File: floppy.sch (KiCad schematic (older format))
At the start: 4 parts, among them CN11 INTERNAL_FLOPPY, CN12 FLOPPY_POWER, U36 74LS05, U5 GARY_5719

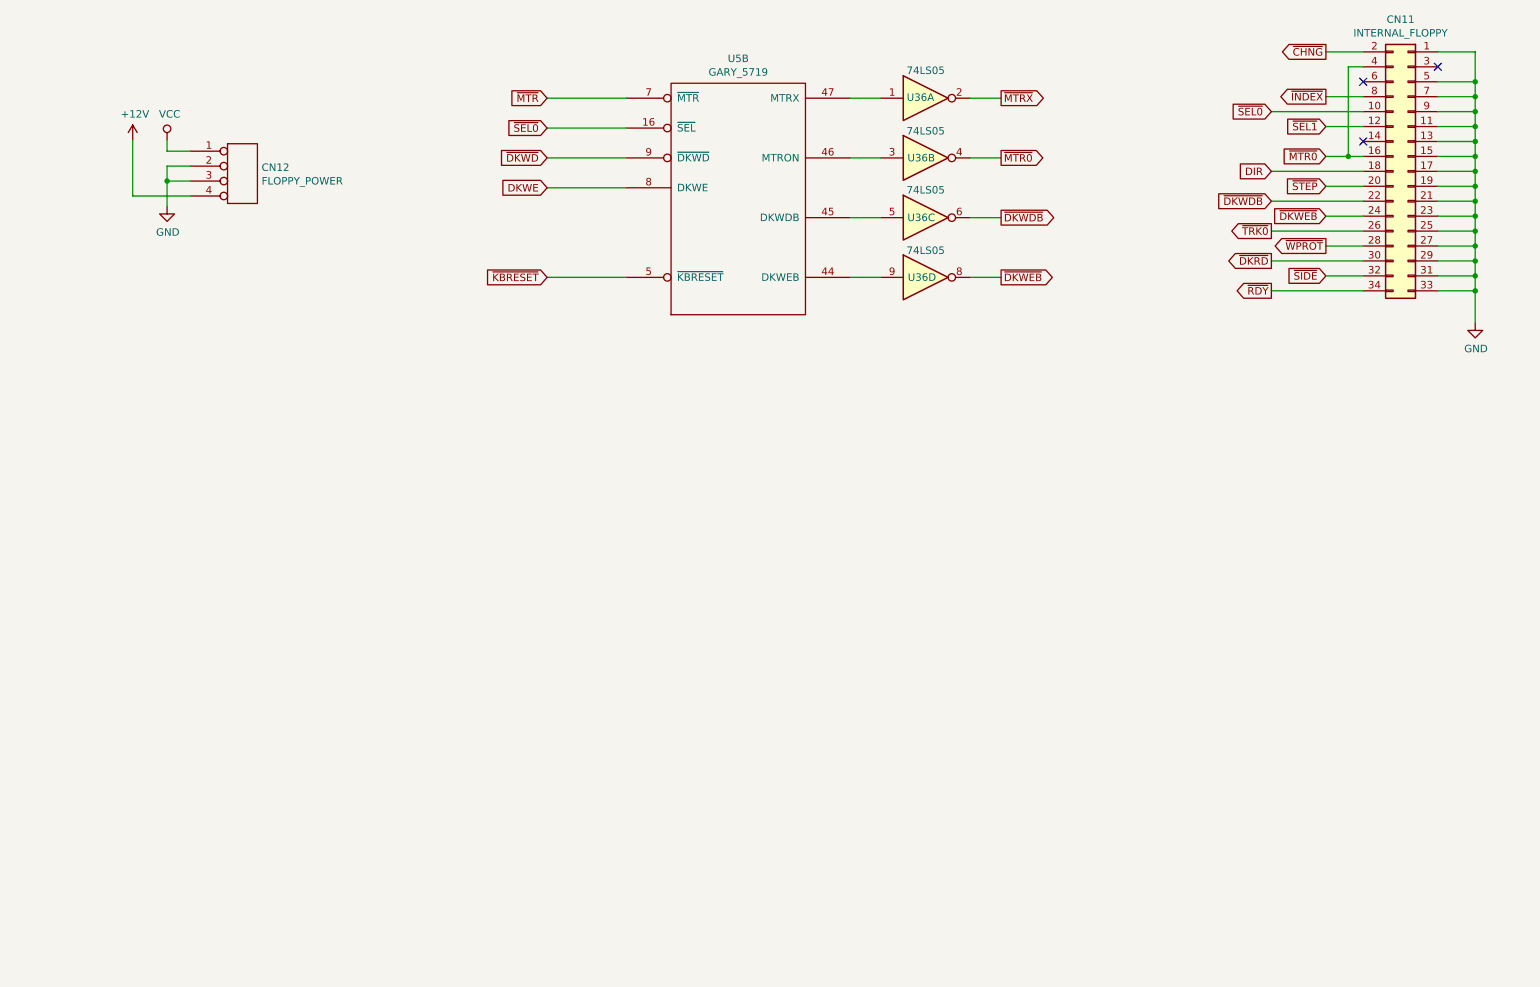
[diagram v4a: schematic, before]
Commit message: Add external floppy connector (and do a few fixes)
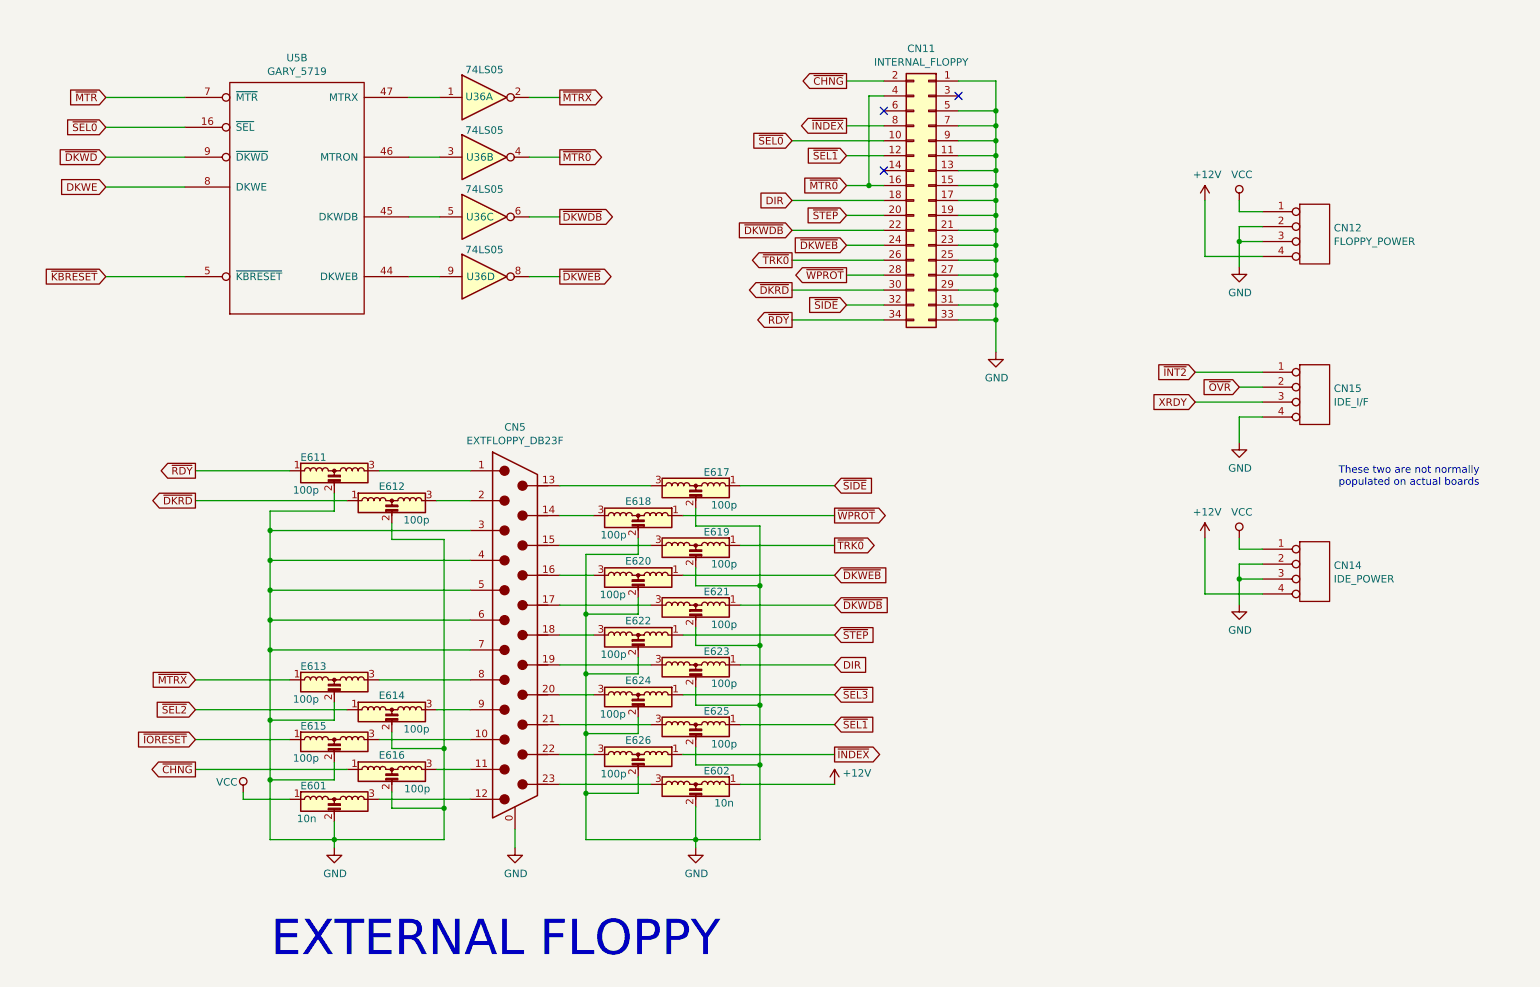
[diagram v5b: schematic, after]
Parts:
- added CN14: IDE_POWER, symbol conn:CONN_4
- added CN15: IDE_I/F, symbol conn:CONN_4
- added CN5: EXTFLOPPY_DB23F, symbol db23_mountingholes_2sides:DB23_MountingHoles_2sides
- added E601, E602: 10n, symbol emi_filter_lcl_small:EMI_Filter_LCL
- added E611, E612, E613, E614, E615, E616, E617, E618, E619, E620, E621, E622, E623, E624, E625, E626: 100p, symbol emi_filter_lcl_small:EMI_Filter_LCL
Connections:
- net +12V: now also CN14.4 (P4), E602.1
- net DIR: now also E623.1
- net GND: now also CN14.2 (P2), CN14.3 (P3), CN15.4 (P4), CN5.0 (PAD), CN5.3, CN5.4, CN5.5, CN5.6, CN5.7, E601.2, E602.2, E611.2, E612.2, E613.2, E614.2, E615.2, E616.2, E617.2, E618.2, E619.2, E620.2, E621.2, E622.2, E623.2, E624.2, E625.2, E626.2
- net VCC: now also CN14.1 (P1), E601.1
- net ~CHNG: now also E616.1
- net ~DKRD: now also E612.1
- net ~DKWDB: now also E621.1
- net ~DKWEB: now also E620.1
- net ~INDEX: now also E626.1
- net ~MTRX: now also E613.1
- net ~RDY: now also E611.1
- net ~SEL1: now also E625.1
- net ~SIDE: now also E617.1
- net ~STEP: now also E622.1
- net ~TRK0: now also E619.1
- net ~WPROT: now also E618.1
- new net: CN5.1, E611.3
- new net: CN5.10, E615.3
- new net: CN5.11, E616.3
- new net: CN5.12, E601.3
- new net: CN5.13 (P13), E617.3
- new net: CN5.14 (P14), E618.3
- new net: CN5.15 (P15), E619.3
- new net: CN5.16 (P16), E620.3
- new net: CN5.17 (P17), E621.3
- new net: CN5.18 (P18), E622.3
- new net: CN5.19 (P19), E623.3
- new net: CN5.2, E612.3
- new net: CN5.20 (P20), E624.3
- new net: CN5.21 (P21), E625.3
- new net: CN5.22 (P22), E626.3
- new net: CN5.23 (P23), E602.3
- new net: CN5.8, E613.3
- new net: CN5.9, E614.3
- new net XRDY: CN15.3 (P3)
- new net ~INT2: CN15.1 (P1)
- new net ~IORESET: E615.1
- new net ~OVR: CN15.2 (P2)
- new net ~SEL2: E614.1
- new net ~SEL3: E624.1
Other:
- note added: "EXTERNAL FLOPPY"
- note added: "These two are not normally\npopulated on actual boards"
- moved on the sheet: CN11, CN12, U36A, U36B, U36C, U36D, U5B

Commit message: Fix power-up reset
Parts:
- CN5: footprint (none) -> Raemixx500:DB_23
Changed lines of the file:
@@
 EESchema Schematic File Version 4
 LIBS:Raemix500-cache
-EELAYER 26 0
+EELAYER 29 0
 EELAYER END
 $Descr A4 11693 8268
@@
 F 0 "CN5" H 4145 3768 50  0000 C CNN
 F 1 "EXTFLOPPY_DB23F" H 4145 3859 50  0000 C CNN
-F 2 "" H 4145 5260 50  0001 C CNN
+F 2 "Raemixx500:DB_23" H 4145 5260 50  0001 C CNN
 F 3 " ~" H 4145 5260 50  0001 C CNN
 	1    4145 5260

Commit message: Work in progress
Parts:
- CN12, CN14, CN15: footprint (none) -> Connector_PinHeader_2.54mm:PinHeader_1x04_P2.54mm_Vertical
- E601, E602: footprint (none) -> Raemixx500:EMI_Filter_Long
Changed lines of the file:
@@
 F 0 "CN12" H 9628 2516 50  0000 L CNN
 F 1 "FLOPPY_POWER" H 9628 2425 50  0000 L CNN
-F 2 "" H 9500 2475 50  0001 C CNN
+F 2 "Connector_PinHeader_2.54mm:PinHeader_1x04_P2.54mm_Vertical" H 9500 2475 50  0001 C CNN
 F 3 "" H 9500 2475 50  0001 C CNN
 	1    9500 2475
@@
 F 0 "E601" H 2795 6550 50  0000 C CNN
 F 1 "10n" H 2750 6330 50  0000 C CNN
-F 2 "" V 2935 6360 50  0001 C CNN
+F 2 "Raemixx500:EMI_Filter_Long" V 2935 6360 50  0001 C CNN
 F 3 "http://www.murata.com/~/media/webrenewal/support/library/catalog/products/emc/emifil/c31e.ashx?la=en-gb" V 2935 6360 50  0001 C CNN
 	1    2935 6360
@@
 F 0 "E602" H 5215 6450 50  0000 C CNN
 F 1 "10n" H 5165 6235 50  0000 C CNN
-F 2 "" V 5355 6260 50  0001 C CNN
+F 2 "Raemixx500:EMI_Filter_Long" V 5355 6260 50  0001 C CNN
 F 3 "http://www.murata.com/~/media/webrenewal/support/library/catalog/products/emc/emifil/c31e.ashx?la=en-gb" V 5355 6260 50  0001 C CNN
 	1    5355 6260
@@
 F 0 "CN15" H 9628 3591 50  0000 L CNN
 F 1 "IDE_I/F" H 9628 3500 50  0000 L CNN
-F 2 "" H 9500 3550 50  0001 C CNN
+F 2 "Connector_PinHeader_2.54mm:PinHeader_1x04_P2.54mm_Vertical" H 9500 3550 50  0001 C CNN
 F 3 "" H 9500 3550 50  0001 C CNN
 	1    9500 3550
@@
 F 0 "CN14" H 9628 4776 50  0000 L CNN
 F 1 "IDE_POWER" H 9628 4685 50  0000 L CNN
-F 2 "" H 9500 4735 50  0001 C CNN
+F 2 "Connector_PinHeader_2.54mm:PinHeader_1x04_P2.54mm_Vertical" H 9500 4735 50  0001 C CNN
 F 3 "" H 9500 4735 50  0001 C CNN
 	1    9500 4735
